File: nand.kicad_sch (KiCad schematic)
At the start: 12 parts, among them U6 IS21ES08GA-JQLI-TR

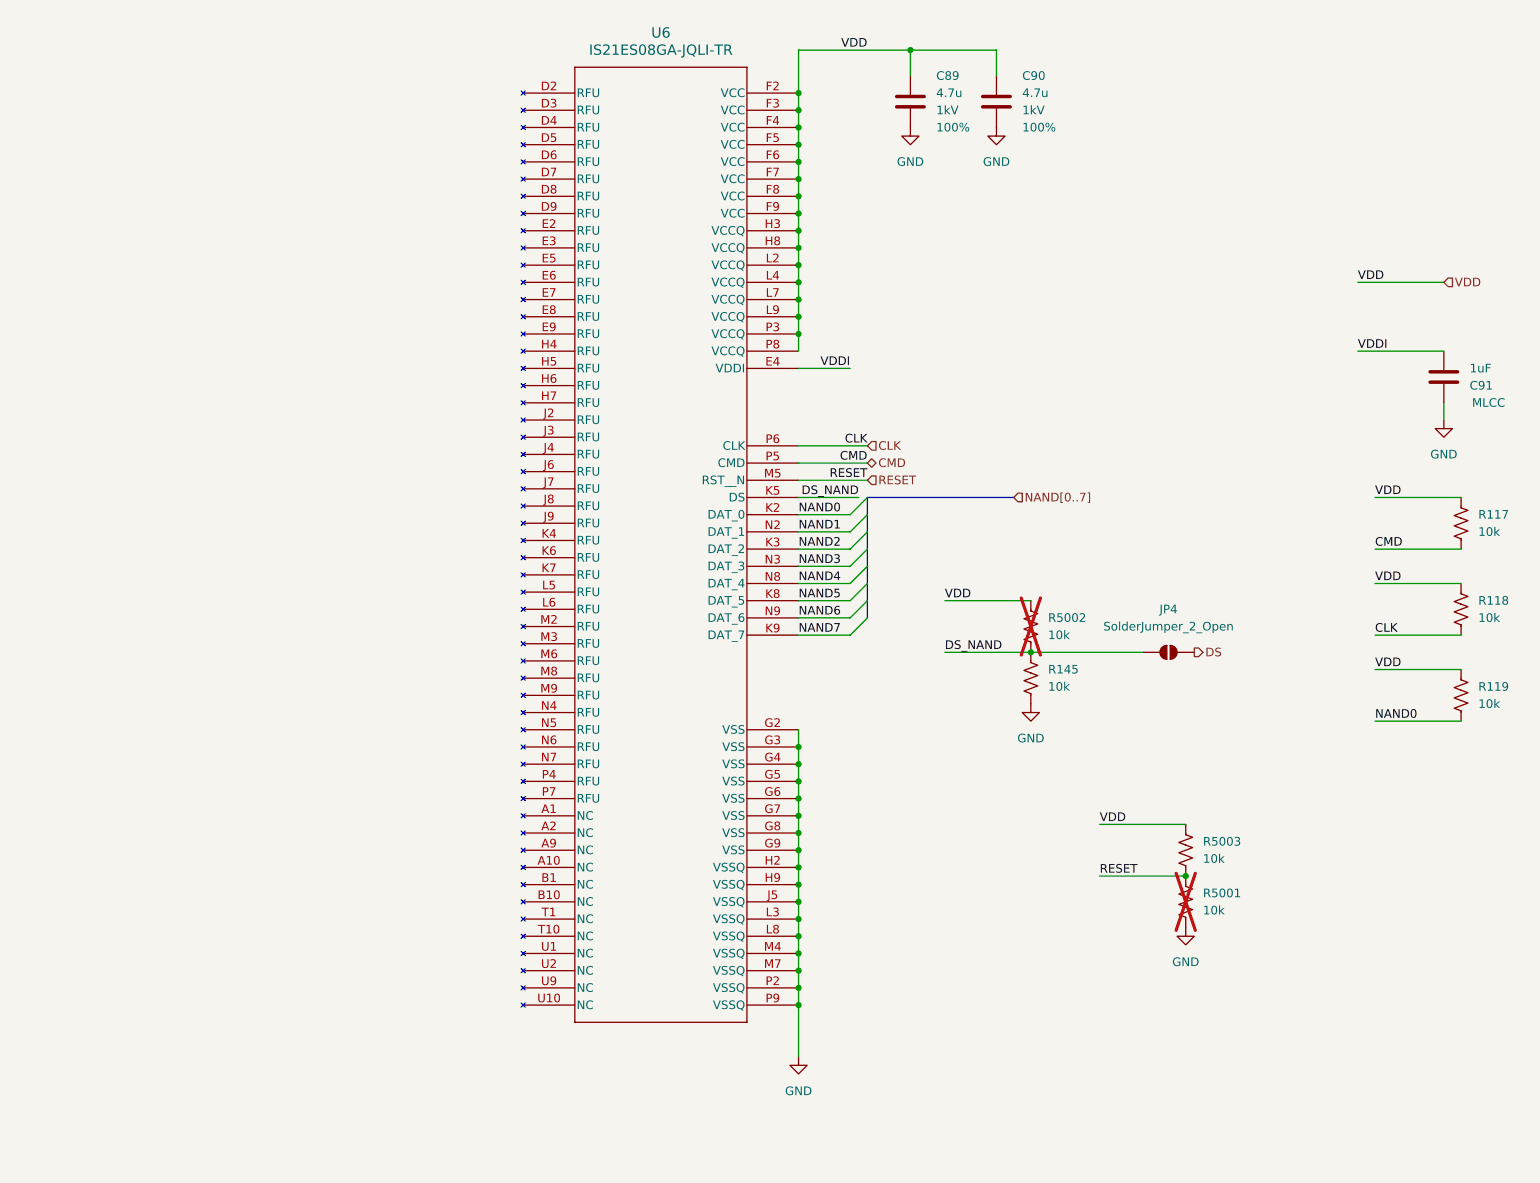
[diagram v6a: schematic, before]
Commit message: Routing eMMC
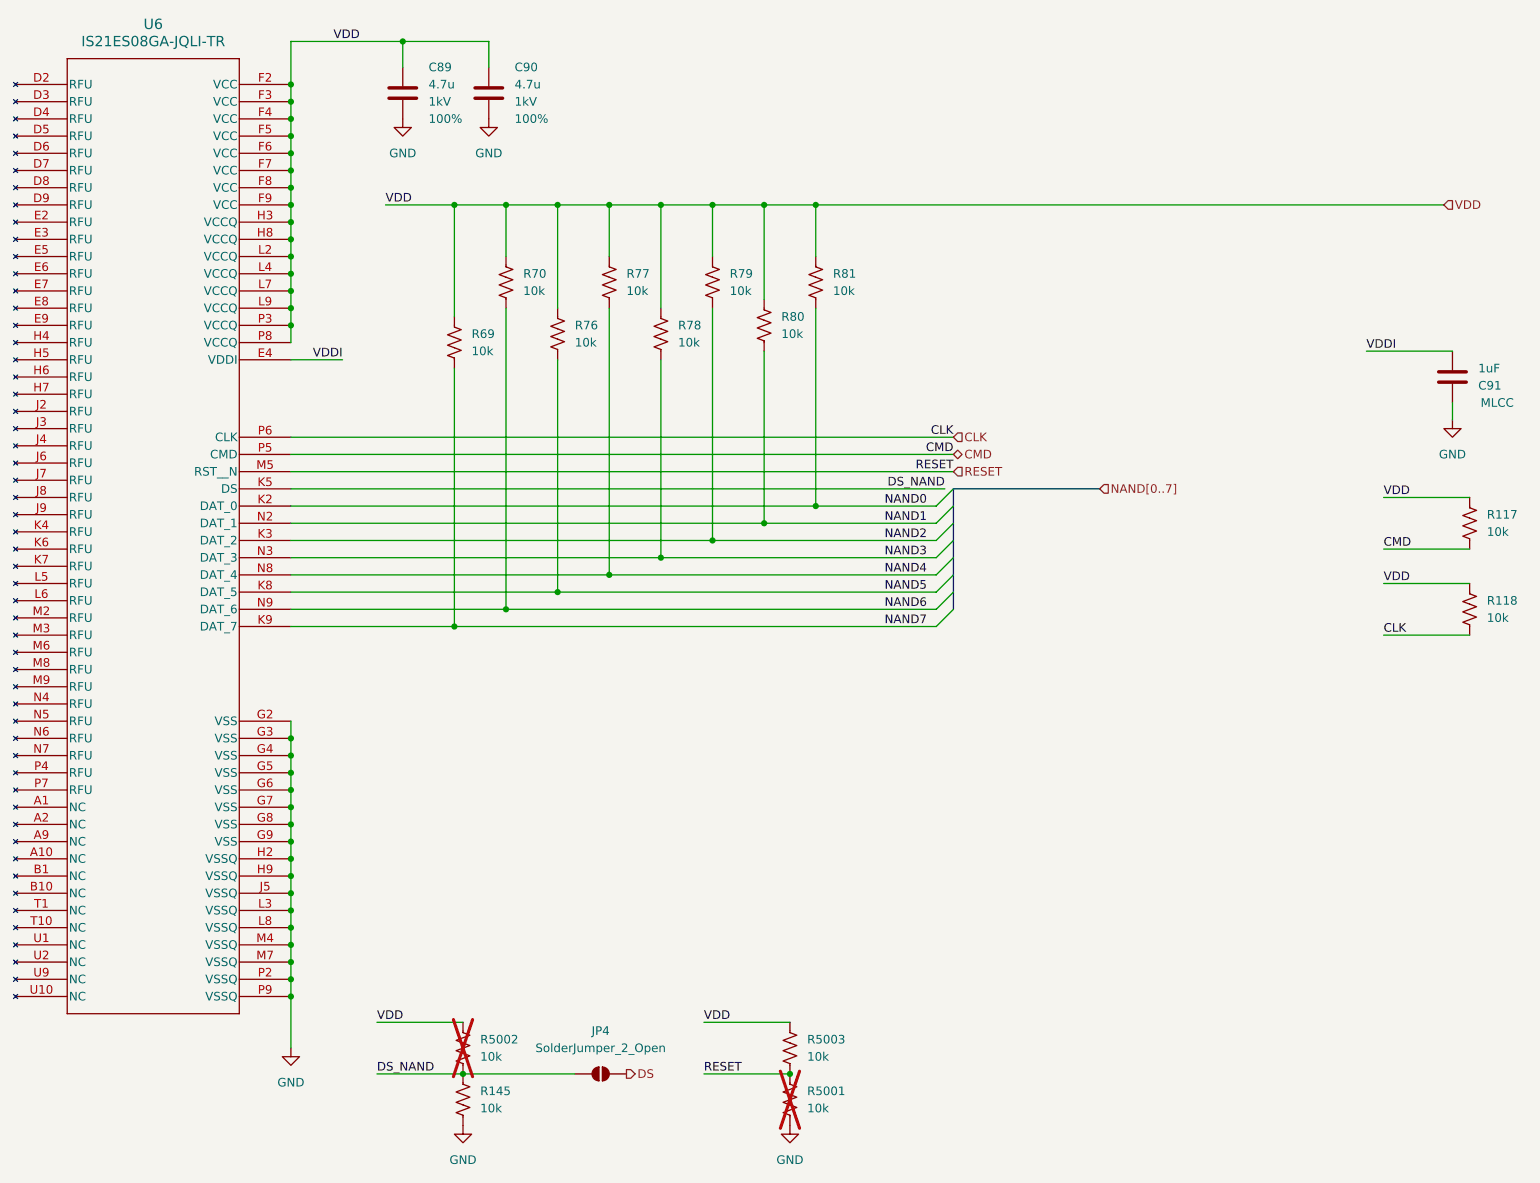
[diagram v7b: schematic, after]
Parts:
- removed R119: 10k, Resistor_SMD:R_0402_1005Metric, symbol SparkFun-Resistor:R
- added R69, R70, R76, R77, R78, R79, R80, R81: 10k, Resistor_SMD:R_0402_1005Metric, symbol SparkFun-Resistor:R
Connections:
- net NAND0: now also R81.2
- net NAND1: now also R80.2
- net NAND2: now also R79.2
- net NAND3: now also R78.2
- net NAND4: now also R77.2
- net NAND5: now also R76.2
- net NAND6: now also R70.2
- net NAND7: now also R69.2
- net VDD: now also R69.1, R70.1, R76.1, R77.1, R78.1, R79.1, R80.1, R81.1
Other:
- moved on the sheet: C89, C90, C91, JP4, R117, R118, R145, R5001, R5002, R5003, U6

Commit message: Routing power
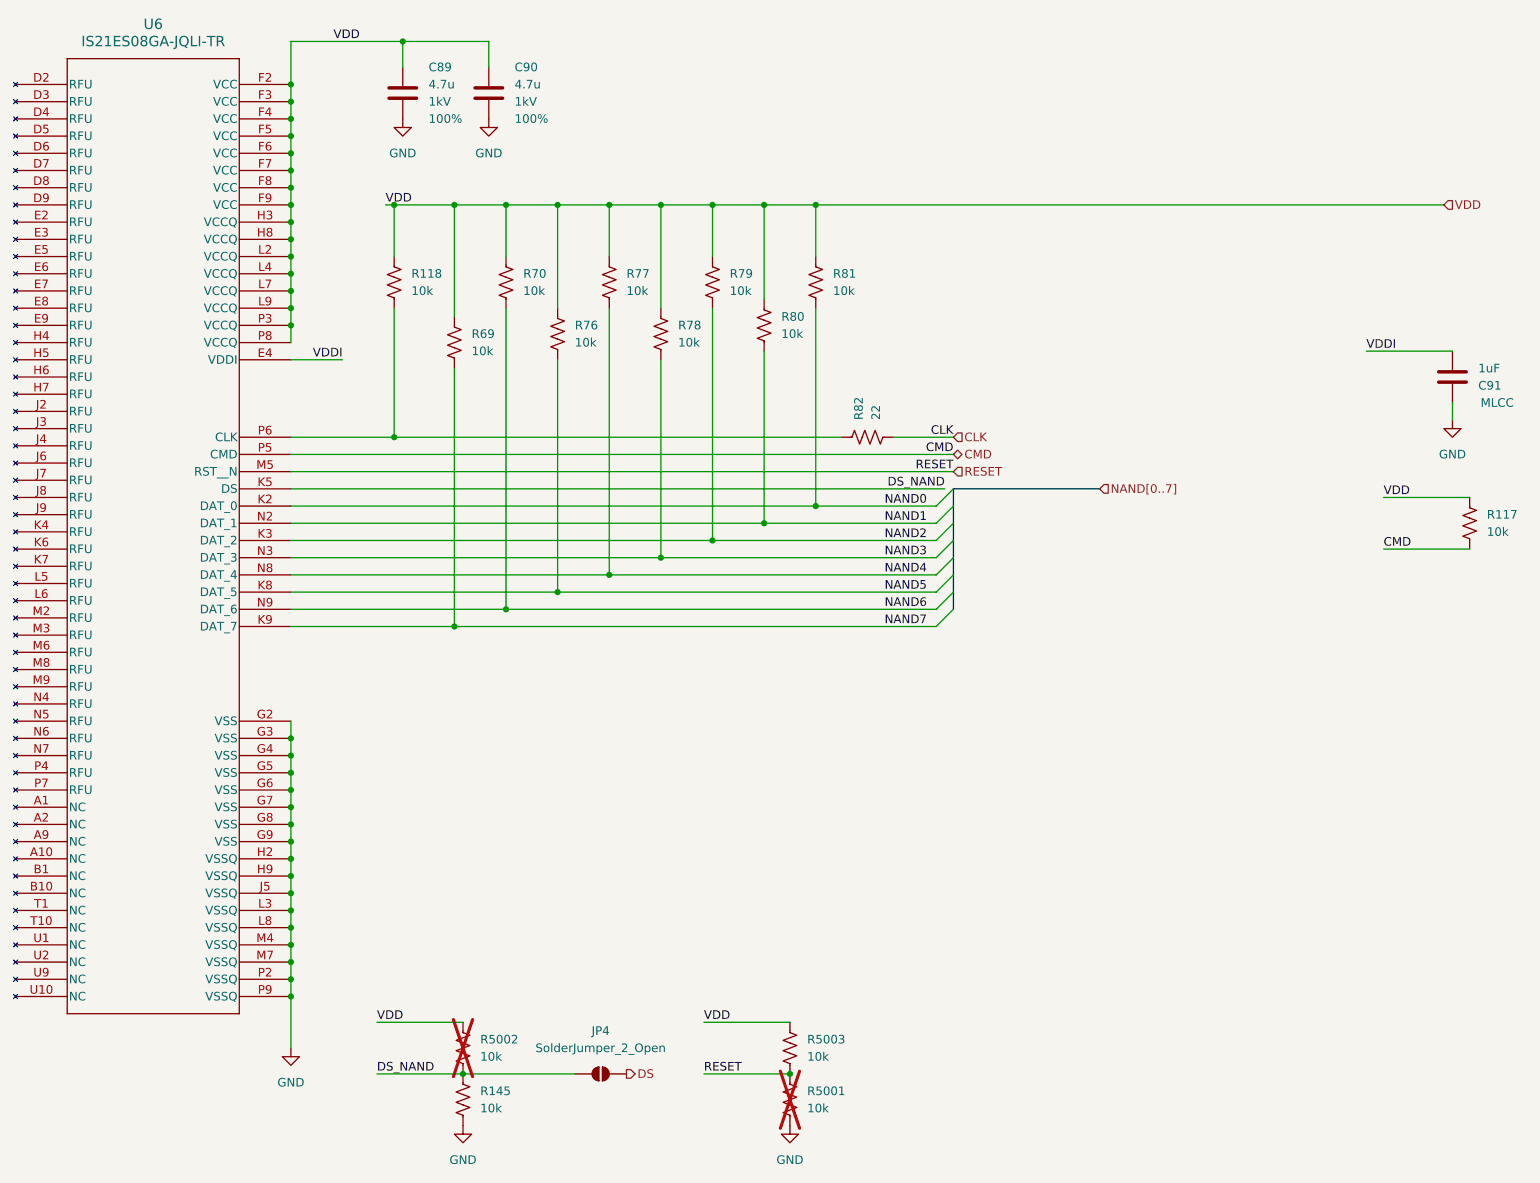
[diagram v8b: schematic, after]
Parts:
- added R82: 22, Resistor_SMD:R_0402_1005Metric, symbol SparkFun-Resistor:R
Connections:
- net CLK: now also R82.2; no longer R118.2, U6.P6 (CLK)
- new net: R118.2, R82.1, U6.P6 (CLK)
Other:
- moved on the sheet: R118
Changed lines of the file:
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@@
+	)
+	(junction
+		(at 99.06 48.26)
+		(diameter 0)
+		(color 0 0 0 0)
 	)
 	(junction
@@
 	(junction
 		(at 146.05 97.79)
+		(diameter 0)
+		(color 0 0 0 0)
+	)
+	(junction
+		(at 99.06 82.55)
 		(diameter 0)
 		(color 0 0 0 0)
@@
 	(wire
 		(pts
-			(xy 245.11 111.76) (xy 257.81 111.76)
-		)
-		(stroke
-			(width 0)
-			(type default)
-		)
-	)
-	(wire
-		(pts
 			(xy 146.05 48.26) (xy 153.67 48.26)
 		)
@@
 	(wire
 		(pts
+			(xy 99.06 63.5) (xy 99.06 82.55)
+		)
+		(stroke
+			(width 0)
+			(type default)
+		)
+	)
+	(wire
+		(pts
 			(xy 245.11 99.06) (xy 257.81 99.06)
 		)
@@
 	(wire
 		(pts
-			(xy 83.82 82.55) (xy 181.61 82.55)
+			(xy 83.82 82.55) (xy 99.06 82.55)
+		)
+		(stroke
+			(width 0)
+			(type default)
+		)
+	)
+	(wire
+		(pts
+			(xy 99.06 82.55) (xy 165.1 82.55)
 		)
 		(stroke
@@
 	(wire
 		(pts
+			(xy 99.06 48.26) (xy 107.95 48.26)
+		)
+		(stroke
+			(width 0)
+			(type default)
+		)
+	)
+	(wire
+		(pts
 			(xy 83.82 100.33) (xy 138.43 100.33)
 		)
@@
 	(wire
 		(pts
+			(xy 99.06 48.26) (xy 99.06 55.88)
+		)
+		(stroke
+			(width 0)
+			(type default)
+		)
+	)
+	(wire
+		(pts
 			(xy 83.82 152.4) (xy 83.82 154.94)
 		)
@@
 	(wire
 		(pts
-			(xy 245.11 104.14) (xy 257.81 104.14)
-		)
-		(stroke
-			(width 0)
-			(type default)
-		)
-	)
-	(wire
-		(pts
 			(xy 113.03 24.13) (xy 113.03 27.94)
 		)
@@
 	(wire
 		(pts
+			(xy 172.72 82.55) (xy 181.61 82.55)
+		)
+		(stroke
+			(width 0)
+			(type default)
+		)
+	)
+	(wire
+		(pts
 			(xy 161.29 48.26) (xy 254 48.26)
 		)
@@
 	(wire
 		(pts
-			(xy 97.79 48.26) (xy 107.95 48.26)
+			(xy 97.79 48.26) (xy 99.06 48.26)
 		)
 		(stroke
@@
 		)
 	)
-	(label "VDD"
-		(at 245.11 104.14 0)
-		(effects
-			(font
-				(size 1.27 1.27)
-			)
-			(justify left bottom)
-		)
-	)
 	(label "CMD"
 		(at 181.61 85.09 180)
@@
 	(label "VDDI"
 		(at 242.57 69.85 0)
-		(effects
-			(font
-				(size 1.27 1.27)
-			)
-			(justify left bottom)
-		)
-	)
-	(label "CLK"
-		(at 245.11 111.76 0)
 		(effects
 			(font
@@
 	(symbol
 		(lib_id "SparkFun-Resistor:R")
-		(at 257.81 107.95 90)
+		(at 99.06 59.69 90)
 		(unit 1)
 		(exclude_from_sim no)
@@
 		(dnp no)
 		(property "Reference" "R118"
-			(at 260.35 106.6799 90)
+			(at 101.6 58.4199 90)
 			(effects
 				(font
@@
 		)
 		(property "Value" "10k"
-			(at 260.35 109.2199 90)
+			(at 101.6 60.9599 90)
 			(effects
 				(font
@@
 		)
 		(property "Footprint" "Resistor_SMD:R_0402_1005Metric"
-			(at 262.382 107.95 0)
+			(at 103.632 59.69 0)
 			(effects
 				(font
@@
 		)
 		(property "Datasheet" ""
-			(at 266.7 109.22 0)
+			(at 107.95 60.96 0)
 			(effects
 				(font
@@
 		)
 		(property "Description" "Resistor"
-			(at 269.24 107.95 0)
+			(at 110.49 59.69 0)
 			(effects
 				(font
@@
 		)
 		(property "Precision" "5%"
-			(at 260.604 111.506 90)
+			(at 101.854 63.246 90)
 			(effects
 				(font
@@
 					(unit 1)
 				)
+			)
+		)
+	)
+	(symbol
+		(lib_id "SparkFun-Resistor:R")
+		(at 168.91 82.55 180)
+		(unit 1)
+		(exclude_from_sim no)
+		(in_bom yes)
+		(on_board yes)
+		(dnp no)
+		(property "Reference" "R82"
+			(at 167.6399 80.01 90)
+			(effects
+				(font
+					(size 1.27 1.27)
+				)
+				(justify right)
+			)
+		)
+		(property "Value" "22"
+			(at 170.1799 80.01 90)
+			(effects
+				(font
+					(size 1.27 1.27)
+				)
+				(justify right)
+			)
+		)
+		(property "Footprint" "Resistor_SMD:R_0402_1005Metric"
+			(at 168.91 77.978 0)
+			(effects
+				(font
+					(size 1.27 1.27)
+				)
+				(hide yes)
+			)
+		)
+		(property "Datasheet" ""
+			(at 170.18 73.66 0)
+			(effects
+				(font
+					(size 1.27 1.27)
+				)
+				(hide yes)
+			)
+		)
+		(property "Description" "Resistor"
+			(at 168.91 71.12 0)
+			(effects
+				(font
+					(size 1.27 1.27)
+				)
+				(hide yes)
+			)
+		)
+		(property "Precision" "5%"
+			(at 172.466 79.756 90)
+			(effects
+				(font
+					(size 1.27 1.27)
+				)
+				(justify right)
+				(hide yes)
+			)
+		)
+		(pin "2"
+		)
+		(pin "1"
+		)
+		(instances
+			(project "SBC"
+				(path "/21bb932a-ec67-4661-9215-0551f718d1c0/dbc4538f-6782-4334-8773-c54462e4bd8b"
+					(reference "R82")
+					(unit 1)
+				)
